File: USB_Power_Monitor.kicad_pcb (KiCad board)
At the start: 4 copper layers, 41 x 20 mm, 41 parts, among them IC1 MCS1826GQTE-05-P, J1 USB_C_Receptacle, J2 USB_C_Plug, J3 OLED, SW1 SW_Push_Dual, U1 RP2040, U2 L7983PU33R, U4 TS3USB221AQRSERQ1

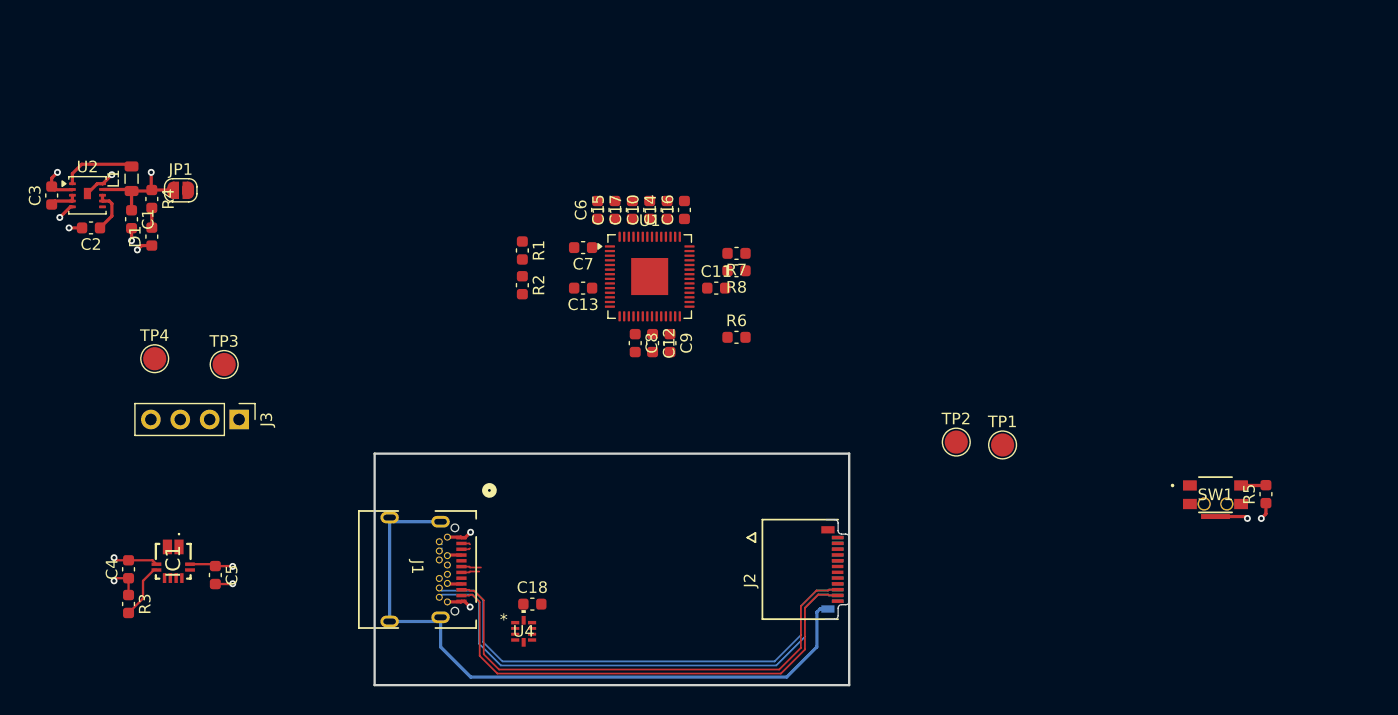
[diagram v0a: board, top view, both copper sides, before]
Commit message: finished routing RP2040
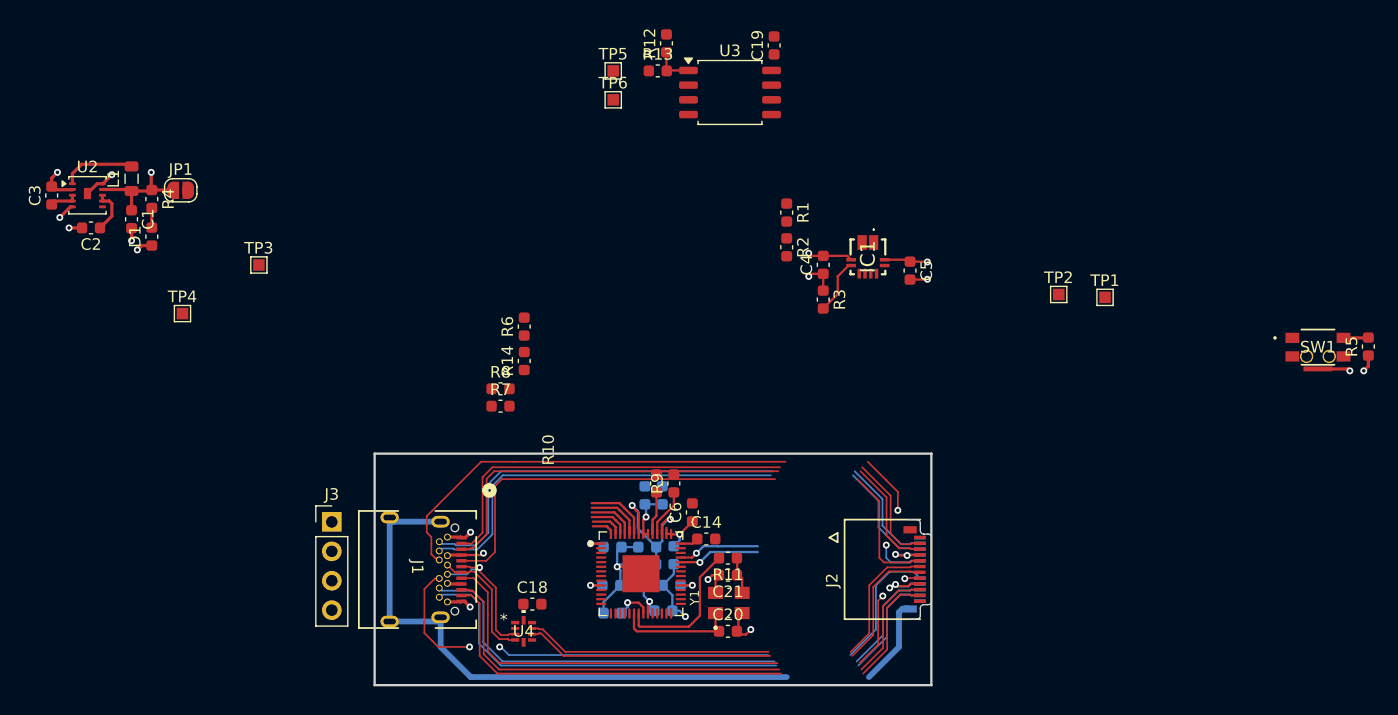
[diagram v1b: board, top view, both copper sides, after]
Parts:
- added C19: 100nF, Capacitor_SMD:C_0603_1608Metric, F.Cu at (161.5, 52.7)
- added C20: 15pF, Capacitor_SMD:C_0603_1608Metric, F.Cu at (157.5, 103.3)
- added C21: 15pF, Capacitor_SMD:C_0603_1608Metric, F.Cu at (157.5, 98.5)
- added R10: 27, Capacitor_SMD:C_0603_1608Metric, F.Cu at (151.3, 90.6)
- added R11: 1kR, Capacitor_SMD:C_0603_1608Metric, F.Cu at (157.5, 97.0)
- added R12: DNF, Capacitor_SMD:C_0603_1608Metric, F.Cu at (152.2, 52.6)
- added R13: 1kR, Capacitor_SMD:C_0603_1608Metric, F.Cu at (151.5, 54.9)
- added R14: DNF, Capacitor_SMD:C_0603_1608Metric, F.Cu at (139.9, 80.0)
- added R9: 27, Capacitor_SMD:C_0603_1608Metric, F.Cu at (152.8, 90.6)
- added TP5: TestPoint, TestPoint:TestPoint_Pad_1.0x1.0mm, F.Cu at (147.6, 54.9)
- added TP6: TestPoint, TestPoint:TestPoint_Pad_1.0x1.0mm, F.Cu at (147.6, 57.4)
- added U3: W25Q16JVSS, Package_SO:SOIC-8_5.3x5.3mm_P1.27mm, F.Cu at (157.7, 56.8)
- added Y1: ABM8-272-T3, ABM8-272-T3:XTAL_ABM8-272-T3, F.Cu at (157.6, 100.9)
- C10, C11, C12, C13, C15, C16, C17, C7, C8, C9: moved to B.Cu
- TP1, TP2, TP3, TP4: footprint TestPoint:TestPoint_Pad_D2.0mm -> TestPoint:TestPoint_Pad_1.0x1.0mm
- moved IC1 65.5 mm to (169.6, 71.0)
- moved C4 65.5 mm to (165.8, 71.7)
- moved C5 65.5 mm to (173.3, 72.2)
- moved R3 65.5 mm to (165.8, 74.7)
- moved C16 34.7 mm to (151.9, 101.6), turned to 0 degrees
- moved C17 30.7 mm to (150.6, 97.6), turned to 180 degrees
- moved C14 28.6 mm to (155.7, 95.4), turned to 0 degrees
- moved C6 27.4 mm to (154.4, 93.1)
- moved C7 26.0 mm to (147.6, 96.1), turned to 0 degrees
- moved C11 26.0 mm to (152.7, 99.4), turned to 180 degrees
- moved C13 25.8 mm to (147.4, 99.4), turned to 0 degrees
- moved U1 25.7 mm to (150.0, 98.4)
- moved C15 25.0 mm to (151.8, 91.6)
- moved C10 24.7 mm to (150.3, 91.6)
- moved R7 24.3 mm to (137.9, 83.9), turned to 0 degrees
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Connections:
- R6 pad 2: GND -> +3.3V
- U1 pad 20: unconnected-(U1-XIN-Pad20) -> /XIN
- U1 pad 21: unconnected-(U1-XOUT-Pad21) -> /XOUT
- U1 pad 46: /RP_D- -> Net-(U1-USB_DM)
- U1 pad 47: /RP_D+ -> Net-(U1-USB_DP)
- U1 pad 51: unconnected-(U1-QSPI_SD3-Pad51) -> /QSPI_SD3
- U1 pad 52: unconnected-(U1-QSPI_SCLK-Pad52) -> /QSPI_SCLK
- U1 pad 53: unconnected-(U1-QSPI_SD0-Pad53) -> /QSPI_SD0
- U1 pad 54: unconnected-(U1-QSPI_SD2-Pad54) -> /QSPI_SD2
- U1 pad 55: unconnected-(U1-QSPI_SD1-Pad55) -> /QSPI_SD1
- U1 pad 56: unconnected-(U1-~{QSPI_SS}-Pad56) -> /QSPI_SS
- U4 pad 6: /button1 -> GND
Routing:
- net /SBU2: track 0.00 -> 50.2 mm, vias 0 -> 2
- net /CC2: track 0.00 -> 47.4 mm, vias 0 -> 2
- net /CC1: track 0.00 -> 44.7 mm
- net /SBU1: track 0.00 -> 44.4 mm, vias 0 -> 2
- net /RX1+: track 0.32 -> 43.6 mm
- net /RX1-: track 0.32 -> 43.6 mm
- net /TX1+: track 0.77 -> 42.8 mm
- net /TX1-: track 0.77 -> 42.8 mm
- net /D-: track 0.00 -> 32.7 mm
- net /D+: track 0.00 -> 32.7 mm
- net GND: track 22.4 -> 46.9 mm, vias 10 -> 14
- net +3.3V: track 8.05 -> 28.1 mm, vias 3 -> 9
- net /DVDD: track 0.00 -> 19.3 mm, vias 0 -> 3
- net /XOUT: track 0.00 -> 12.4 mm
- net /XIN: track 0.00 -> 10.8 mm
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- added copper zone on In1.Cu, net GND
- added copper zone on In2.Cu, net GND
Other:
- board size 41 x 20 mm -> 48.1 x 20 mm

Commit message: finished routing most components, no power yet
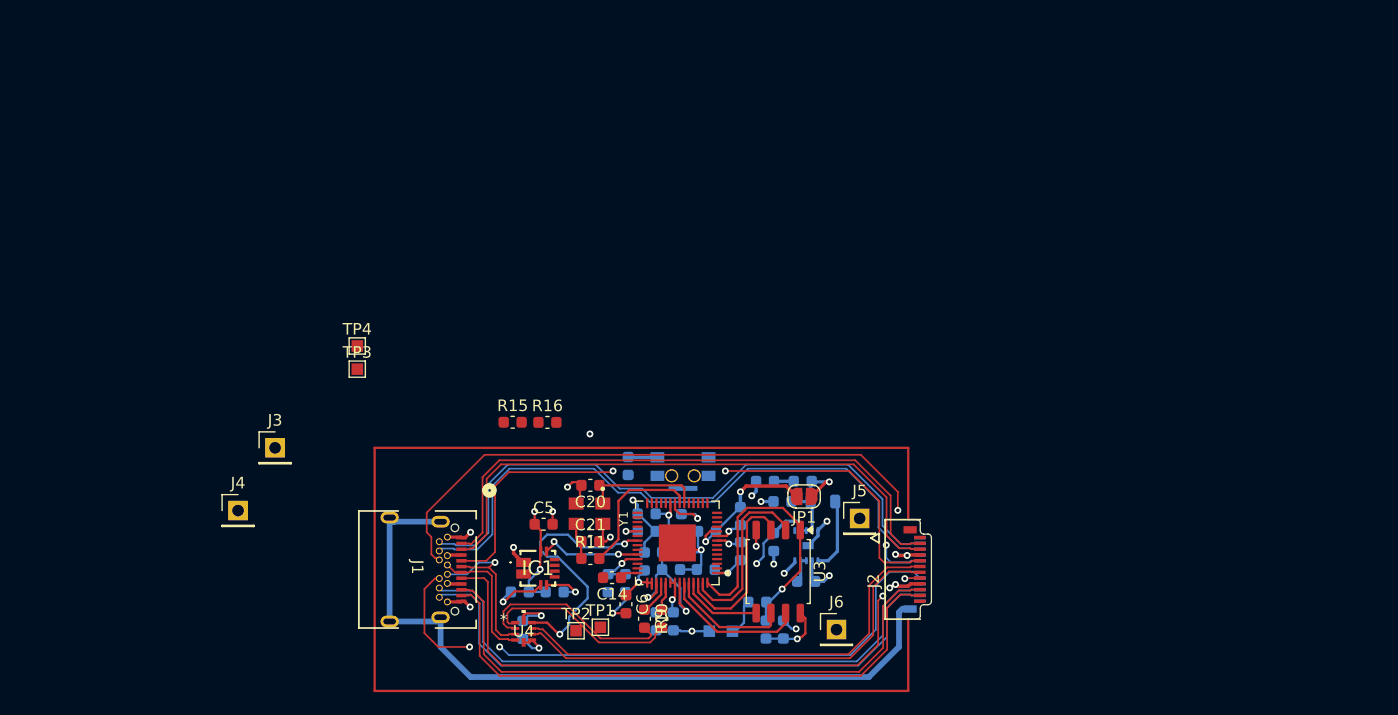
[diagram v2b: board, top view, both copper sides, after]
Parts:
- removed R14: DNF, Capacitor_SMD:C_0603_1608Metric
- removed R6: 2.2kR, Capacitor_SMD:C_0603_1608Metric
- added J4: Conn_01x01, Connector_PinHeader_2.54mm:PinHeader_1x01_P2.54mm_Vertical, F.Cu at (115.2, 92.9)
- added J5: Conn_01x01, Connector_PinHeader_2.54mm:PinHeader_1x01_P2.54mm_Vertical, F.Cu at (168.9, 93.6)
- added J6: Conn_01x01, Connector_PinHeader_2.54mm:PinHeader_1x01_P2.54mm_Vertical, F.Cu at (166.9, 103.2)
- added R15: DNF, Capacitor_SMD:C_0603_1608Metric, F.Cu at (138.9, 85.3)
- added R16: 2.2kR, Capacitor_SMD:C_0603_1608Metric, F.Cu at (141.9, 85.3)
- C1, C18, C19, C2, C3, C4, D1, L1, R1, R12, R13, R2, R3, R4, R5, R7, R8, SW1, TP5, TP6, U2: moved to B.Cu
- J3: value OLED -> Conn_01x01; footprint Connector_PinHeader_2.54mm:PinHeader_1x04_P2.54mm_Vertical -> Connector_PinHeader_2.54mm:PinHeader_1x01_P2.54mm_Vertical
- moved C3 73.2 mm to (164.3, 99.0), turned to 0 degrees
- moved U2 69.1 mm to (164.3, 96.0), turned to 90 degrees
- moved L1 65.9 mm to (165.7, 92.1), turned to 0 degrees
- moved C2 64.9 mm to (161.5, 95.6), turned to -90 degrees
- moved R5 64.8 mm to (148.9, 89.1)
- moved C1 61.3 mm to (162.2, 92.1), turned to 180 degrees
- moved R4 61.3 mm to (164.0, 90.4), turned to 180 degrees
- moved JP1 60.0 mm to (164.1, 91.7), turned to 180 degrees
- moved D1 57.0 mm to (160.7, 90.4), turned to 0 degrees
- moved SW1 55.8 mm to (153.6, 89.1), turned to 180 degrees
- moved TP1 52.1 mm to (146.5, 103.0)
- moved R12 51.4 mm to (160.8, 103.2), turned to -90 degrees
- moved TP2 50.8 mm to (144.4, 103.3)
- moved C19 50.5 mm to (162.3, 103.2)
- moved TP5 49.5 mm to (157.9, 103.3), turned to -90 degrees
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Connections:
- U1 pad 14: /USB_S -> unconnected-(U1-GPIO11-Pad14)
- U1 pad 35: unconnected-(U1-GPIO23-Pad35) -> /USB_S
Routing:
- net +3.3V: track 28.1 -> 52.3 mm, vias 9 -> 12
- net /USB_S: track 0.00 -> 23.5 mm, vias 0 -> 2
- net /QSPI_SS: track 5.51 -> 25.3 mm, vias 0 -> 1
- net /RP_D-: track 0.00 -> 17.5 mm
- net /RP_D+: track 0.00 -> 16.9 mm
- net /QSPI_SD1: track 2.75 -> 15.6 mm
- net /QSPI_SD2: track 4.20 -> 15.3 mm
- net VBUS_SRC: track 13.8 -> 24.6 mm, vias 4 -> 6
- net GND: track 46.9 -> 57.3 mm, vias 14 -> 18
- net /RX1-: track 43.6 -> 53.6 mm
- net /RX1+: track 43.6 -> 53.6 mm
- net /CC1: track 44.7 -> 52.8 mm, vias 0 -> 2
- net /SBU1: track 44.4 -> 52.2 mm
- net /SBU2: track 50.2 -> 58.0 mm
- net /TX1-: track 42.8 -> 50.4 mm
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- added copper zone on In1.Cu, net VBUS_DEV
- added copper zone on In2.Cu, net VBUS_DEV
- removed copper zone on In2.Cu, net GND
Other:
- board size 48.1 x 20 mm -> 2 x 8.6 mm

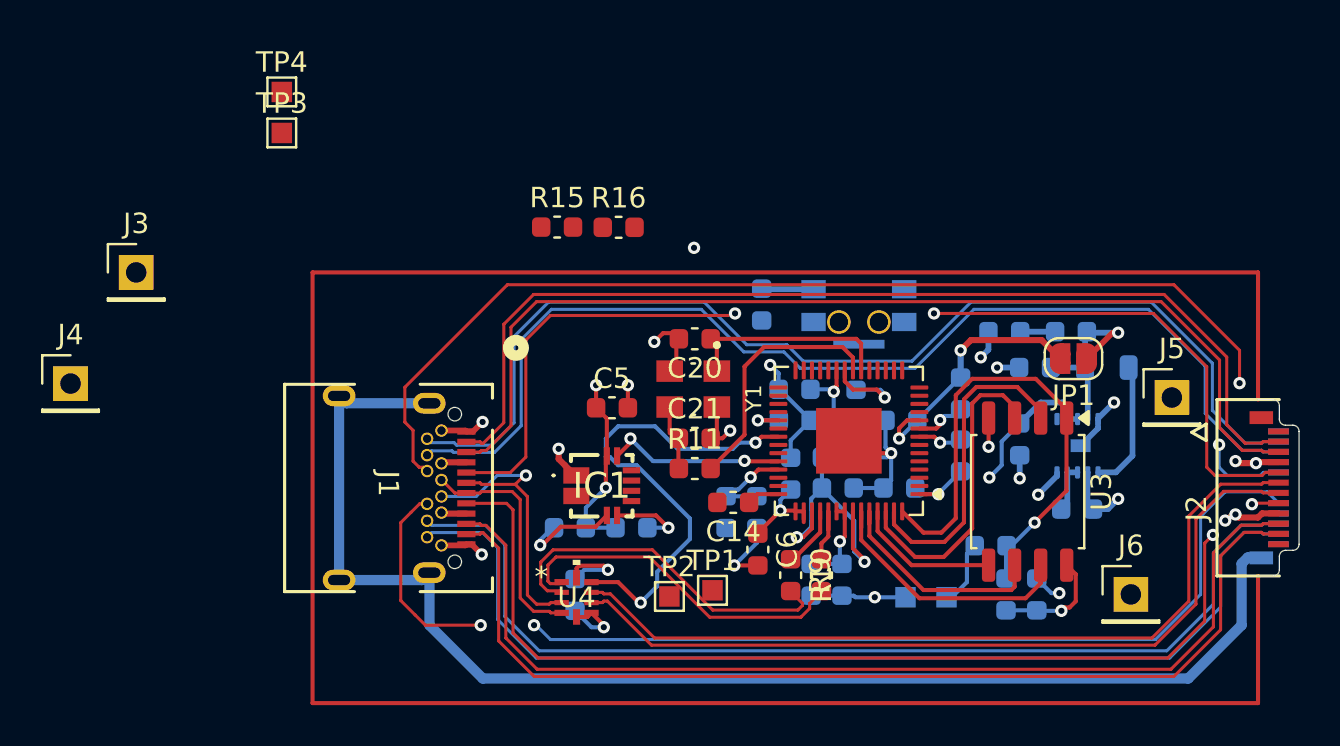
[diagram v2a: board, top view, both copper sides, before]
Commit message: Main power zone defined
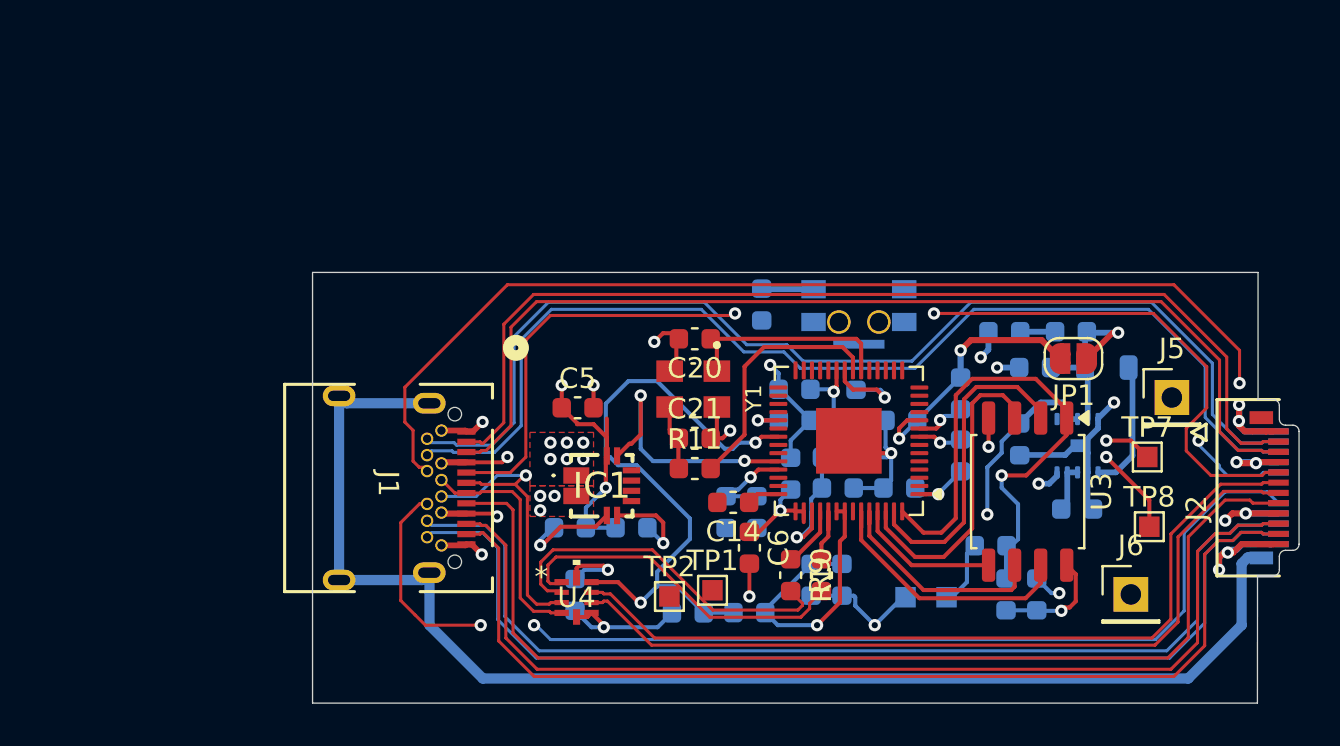
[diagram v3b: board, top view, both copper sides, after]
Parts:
- removed J3, J4: Conn_01x01, Connector_PinHeader_2.54mm:PinHeader_1x01_P2.54mm_Vertical
- removed TP3, TP4: TestPoint, TestPoint:TestPoint_Pad_1.0x1.0mm
- added TP7: TestPoint, TestPoint:TestPoint_Pad_1.0x1.0mm, F.Cu at (167.7, 96.5)
- added TP8: TestPoint, TestPoint:TestPoint_Pad_1.0x1.0mm, F.Cu at (167.8, 99.9)
- R15, R16: moved to B.Cu
- moved R15 19.9 mm to (145.3, 104.1)
- moved R16 19.8 mm to (148.3, 104.1)
- moved C5 1.67 mm to (139.9, 94.1)
- moved C6 0.42 mm to (148.3, 100.9)
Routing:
- net GND: track 57.3 -> 76.2 mm, vias 18 -> 20
- net /SDA: track 2.19 -> 15.4 mm, vias 1 -> 2
- net +3.3V: track 52.3 -> 64.9 mm, vias 12 -> 11
- net /SCL: track 2.66 -> 13.5 mm, vias 1 -> 2
- net /DVDD: track 19.1 -> 12.0 mm, vias 3 -> 2
- net /USB_S: track 23.5 -> 30.6 mm
- net VBUS_SRC: track 24.6 -> 17.5 mm, vias 6 -> 11
- net /Vcurr: track 8.80 -> 13.1 mm
- net VBUS_DEV: track 2.47 -> 6.14 mm, vias 0 -> 5
- net /QSPI_SS: track 25.3 -> 26.7 mm
- net /CC1: track 52.8 -> 53.7 mm
- net /SBU2: track 58.0 -> 58.8 mm
- net Net-(IC1-~{OCD}): track 3.77 -> 4.48 mm
- net /SBU1: track 52.2 -> 52.4 mm, vias 2 -> 0
- added copper zone on F.Cu, net VBUS_DEV
- added copper zone on F.Cu, net VBUS_SRC
- added copper zone on In1.Cu, net VBUS_SRC
- added copper zone on In2.Cu, net VBUS_SRC
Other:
- board size 2 x 8.6 mm -> 46.1 x 21 mm

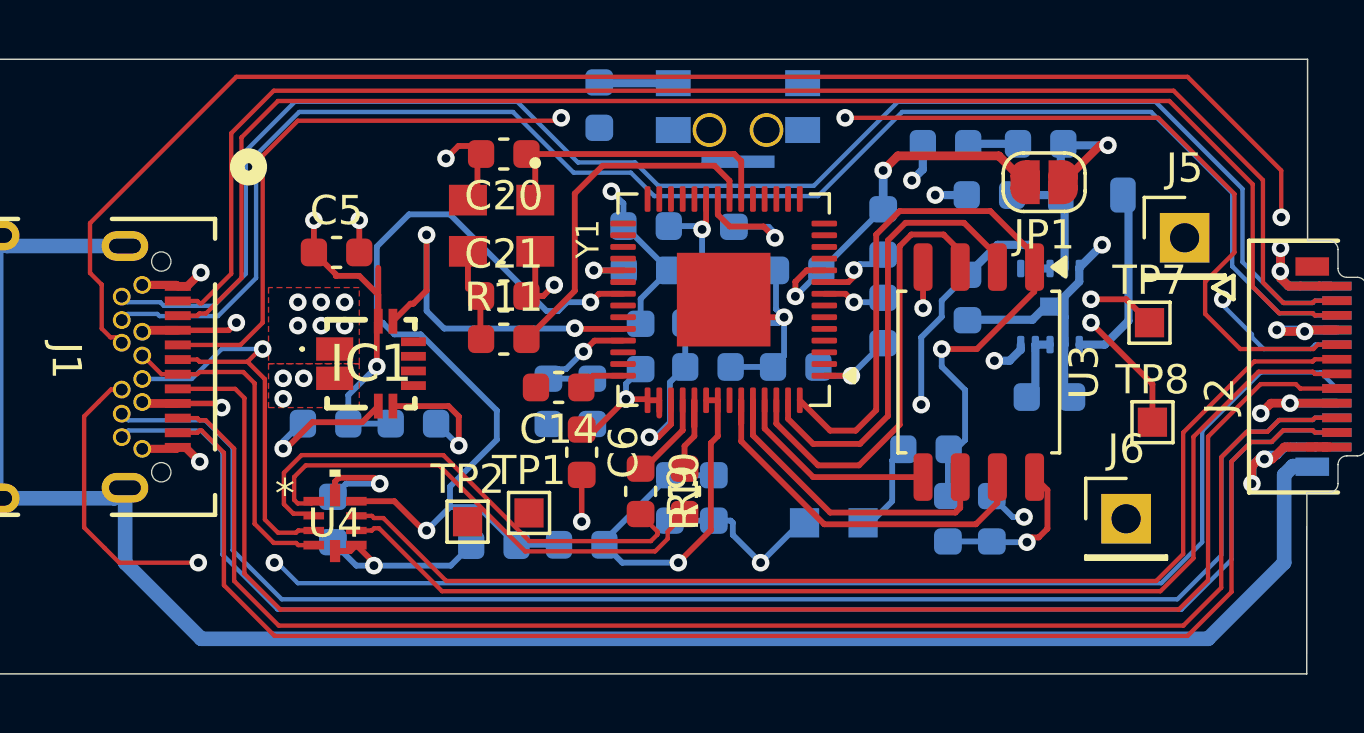
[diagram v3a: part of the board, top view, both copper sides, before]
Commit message: All nets routed, need to clean up text and check errors
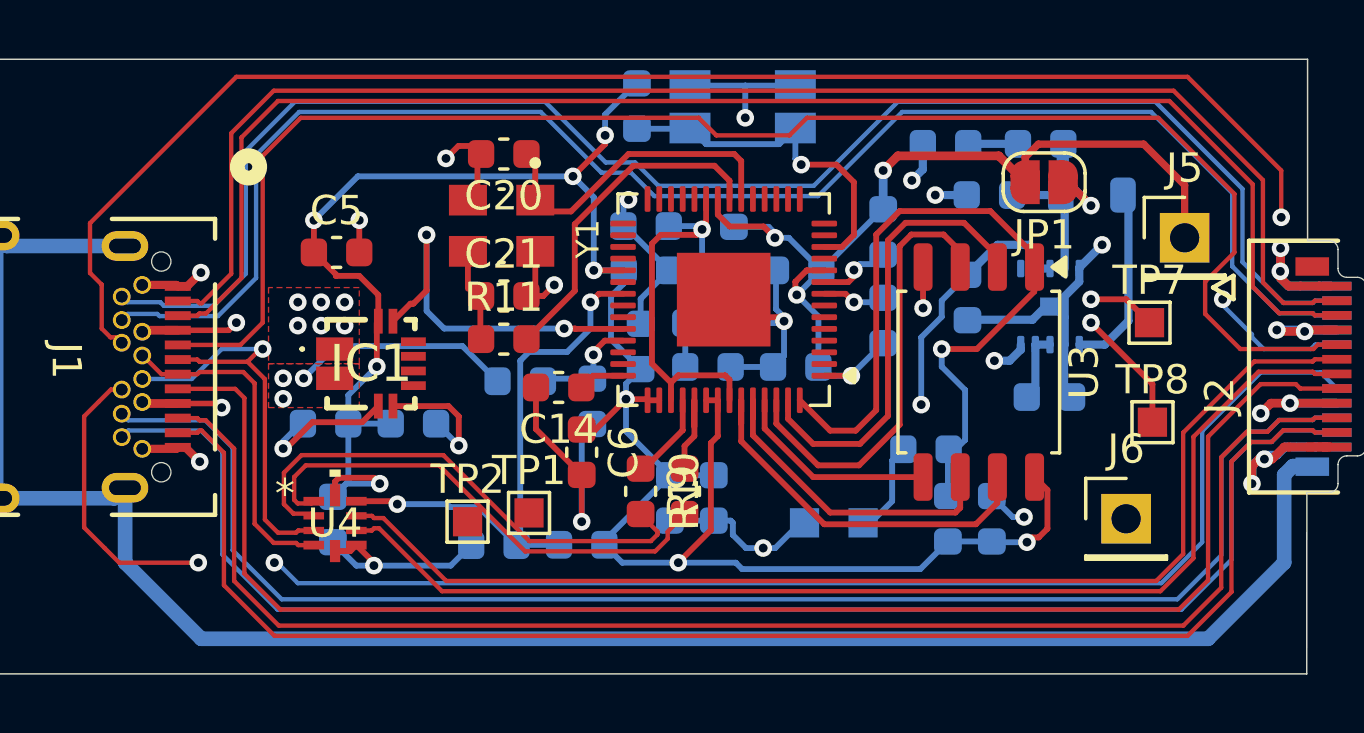
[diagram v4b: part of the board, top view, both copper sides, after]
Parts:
- removed SW1: SW_Push_Dual, KMS231GPLFS:SMT_231GPLFS
- added S1: EVQ-P7A01P, EVQ-P7A01P:SW_EVQ-P7A01P, B.Cu at (153.8, 89.1)
- moved R5 1.29 mm to (150.2, 89.1), turned to -90 degrees
- moved R1 1.18 mm to (146.2, 98.5), turned to 0 degrees
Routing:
- net +3.3V: track 64.9 -> 112.8 mm, vias 11 -> 13
- net /USB_S: track 30.6 -> 18.9 mm
- net GND: track 76.2 -> 87.2 mm, vias 20 -> 21
- net /button1: track 2.84 -> 12.2 mm, vias 0 -> 1
- net VBUS_DEV: track 6.14 -> 13.7 mm
- net /DVDD: track 12.0 -> 17.6 mm, vias 2 -> 1
- net /Vout: track 22.3 -> 20.7 mm
- net /Vmeas: track 4.59 -> 3.60 mm
- net /XOUT: track 12.2 -> 11.6 mm
- net /CC1: track 53.7 -> 53.8 mm, vias 2 -> 0
- added copper zone on In2.Cu, net GND
